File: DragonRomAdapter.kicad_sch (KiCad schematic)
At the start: 8 parts, among them J1 Conn_01x01_Male, U1 68A364, U2 74LVC1G00, U3 28C256

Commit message: tidy-up board
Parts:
- added JP2: Jumper_2_Open, Jumper:SolderJumper-2_P1.3mm_Open_TrianglePad1.0x1.5mm, symbol Jumper:Jumper_2_Open
- J1: now left out of the parts list
- R2, U2: Note (none) -> Not required if JP2 bridged
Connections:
- net ~{E17}: now also JP2.1 (A)
- net ~{E}: now also JP2.2 (B)
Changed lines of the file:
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@@
   )
   (no_connect (at 175.5648 76.3016))
+  (wire (pts (xy 144.8816 24.384) (xy 142.2908 24.384))
+    (stroke (width 0) (type default) (color 0 0 0 0))
+  )
+  (wire (pts (xy 132.1308 24.384) (xy 130.9116 24.384))
+    (stroke (width 0) (type default) (color 0 0 0 0))
+  )
   (wire (pts (xy 136.906 72.644) (xy 137.3124 72.644))
     (stroke (width 0) (type default) (color 0 0 0 0))
@@
   )
   (wire (pts (xy 137.3124 75.438) (xy 137.3124 72.644))
+    (stroke (width 0) (type default) (color 0 0 0 0))
+  )
+  (wire (pts (xy 130.9116 24.384) (xy 130.9116 37.0332))
+    (stroke (width 0) (type default) (color 0 0 0 0))
+  )
+  (wire (pts (xy 144.8816 38.3032) (xy 144.8816 24.384))
     (stroke (width 0) (type default) (color 0 0 0 0))
   )
@@
       (effects (font (size 1.27 1.27)) hide)
     )
+    (property "Note" "Not required if JP2 bridged" (id 4) (at 138.5316 38.3032 0)
+      (effects (font (size 1.27 1.27)) hide)
+    )
     (pin "1")
     (pin "2")
@@
     (pin "1")
   )
+  (symbol (lib_id "Jumper:Jumper_2_Open") (at 137.2108 24.384 0) (unit 1)
+    (in_bom no) (on_board yes) (fields_autoplaced)
+    (property "Reference" "JP2" (id 0) (at 137.2108 17.78 0))
+    (property "Value" "Jumper_2_Open" (id 1) (at 137.2108 20.32 0))
+    (property "Footprint" "Jumper:SolderJumper-2_P1.3mm_Open_TrianglePad1.0x1.5mm" (id 2) (at 137.2108 24.384 0)
+      (effects (font (size 1.27 1.27)) hide)
+    )
+    (property "Datasheet" "~" (id 3) (at 137.2108 24.384 0)
+      (effects (font (size 1.27 1.27)) hide)
+    )
+    (pin "1")
+    (pin "2")
+  )
   (symbol (lib_id "Device:R_Small") (at 134.7724 75.438 270) (unit 1)
     (in_bom yes) (on_board yes)
@@
       (effects (font (size 1.27 1.27)) hide)
     )
+    (property "Note" "Not required if JP2 bridged" (id 4) (at 134.7724 75.438 90)
+      (effects (font (size 1.27 1.27)) hide)
+    )
     (pin "1")
     (pin "2")
@@
   )
   (symbol (lib_id "Connector:Conn_01x01_Male") (at 131.826 72.644 0) (unit 1)
-    (in_bom yes) (on_board yes) (fields_autoplaced)
+    (in_bom no) (on_board yes) (fields_autoplaced)
     (property "Reference" "J1" (id 0) (at 132.461 66.7512 0))
     (property "Value" "Conn_01x01_Male" (id 1) (at 132.461 69.2912 0))
@@
       (reference "JP1") (unit 1) (value "Jumper_3_Bridged12") (footprint "Connector_PinHeader_2.54mm:PinHeader_1x03_P2.54mm_Horizontal")
     )
+    (path "/3828845b-85a6-4ec7-badf-afc34b0893bb"
+      (reference "JP2") (unit 1) (value "Jumper_2_Open") (footprint "Jumper:SolderJumper-2_P1.3mm_Open_TrianglePad1.0x1.5mm")
+    )
     (path "/8595fc95-a608-4da1-ae14-3fc92ad0137b"

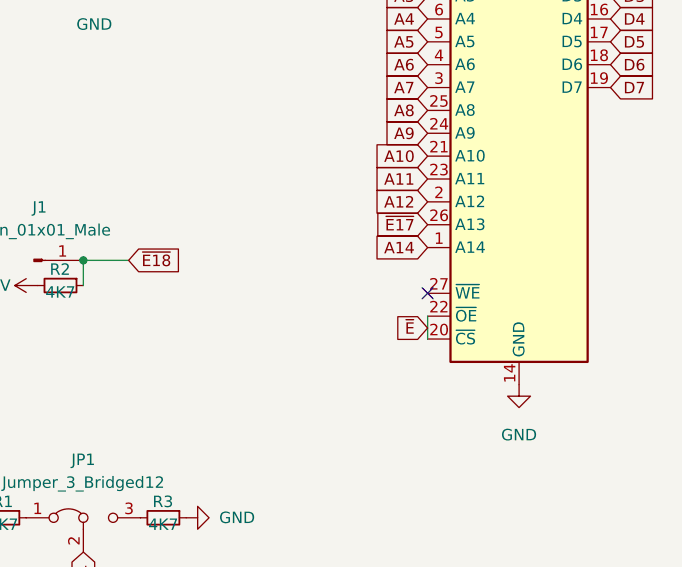
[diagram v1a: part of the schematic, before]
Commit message: use acht logic instead of LVC
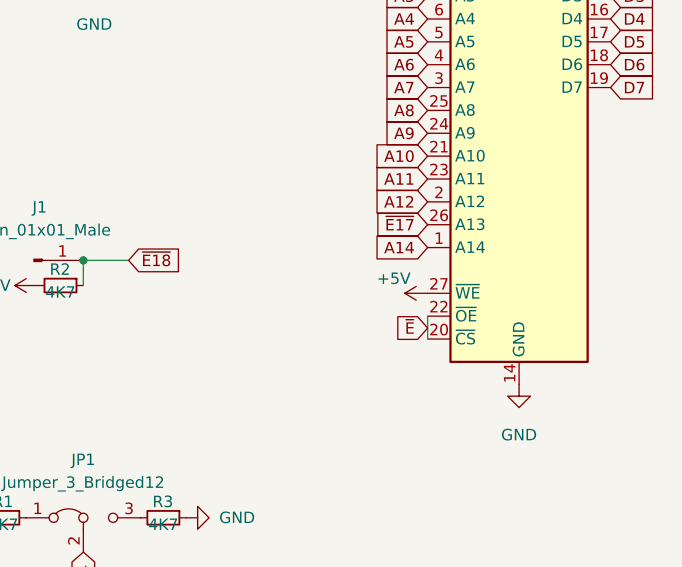
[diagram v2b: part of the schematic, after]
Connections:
- net +5V: now also U3.27 (~{WE})
- no-connect marks 1 -> 0
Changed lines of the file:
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@@
   (junction (at 137.3124 72.644) (diameter 0) (color 0 0 0 0)
   )
-  (no_connect (at 175.5648 76.3016))
   (wire (pts (xy 144.8816 24.384) (xy 142.2908 24.384))
     (stroke (width 0) (type default) (color 0 0 0 0))
@@
     (pin "3")
   )
+  (symbol (lib_id "power:+5V") (at 175.5648 76.3016 90) (unit 1)
+    (in_bom yes) (on_board yes)
+    (property "Reference" "#PWR?" (id 0) (at 179.3748 76.3016 0)
+      (effects (font (size 1.27 1.27)) hide)
+    )
+    (property "Value" "+5V" (id 1) (at 169.926 74.676 90)
+      (effects (font (size 1.27 1.27)) (justify right))
+    )
+    (property "Footprint" "" (id 2) (at 175.5648 76.3016 0)
+      (effects (font (size 1.27 1.27)) hide)
+    )
+    (property "Datasheet" "" (id 3) (at 175.5648 76.3016 0)
+      (effects (font (size 1.27 1.27)) hide)
+    )
+    (pin "1")
+  )
   (symbol (lib_id "Device:R_Small") (at 128.4224 101.2444 270) (unit 1)
     (in_bom yes) (on_board yes)
@@
       (reference "#PWR0106") (unit 1) (value "+5V") (footprint "")
     )
+    (path "/5e38ea97-3af7-4f1d-97a5-960f32b8d19a"
+      (reference "#PWR?") (unit 1) (value "+5V") (footprint "")
+    )
     (path "/9839a238-6b00-4e40-8428-3535b25b1d51"

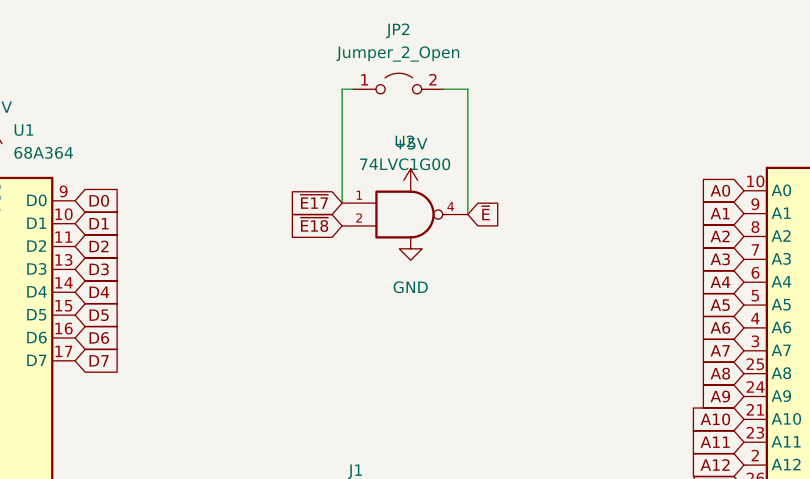
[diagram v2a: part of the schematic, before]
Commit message: migrate to kicad 7
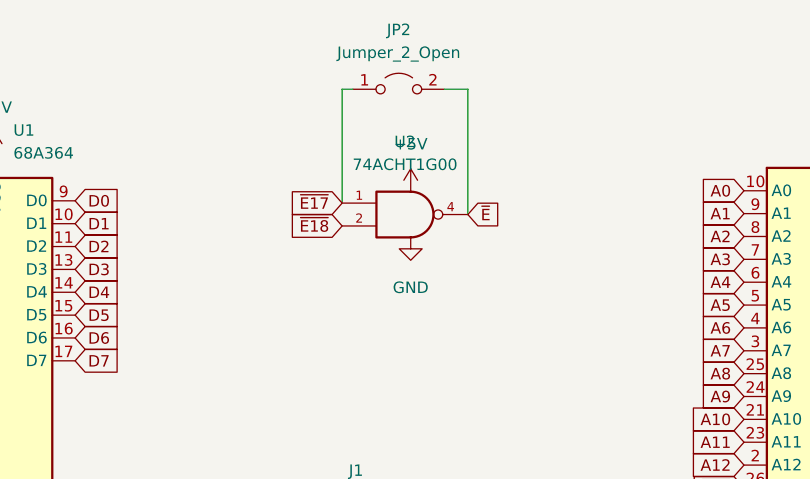
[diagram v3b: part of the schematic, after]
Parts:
- U2: value 74LVC1G00 -> 74ACHT1G00

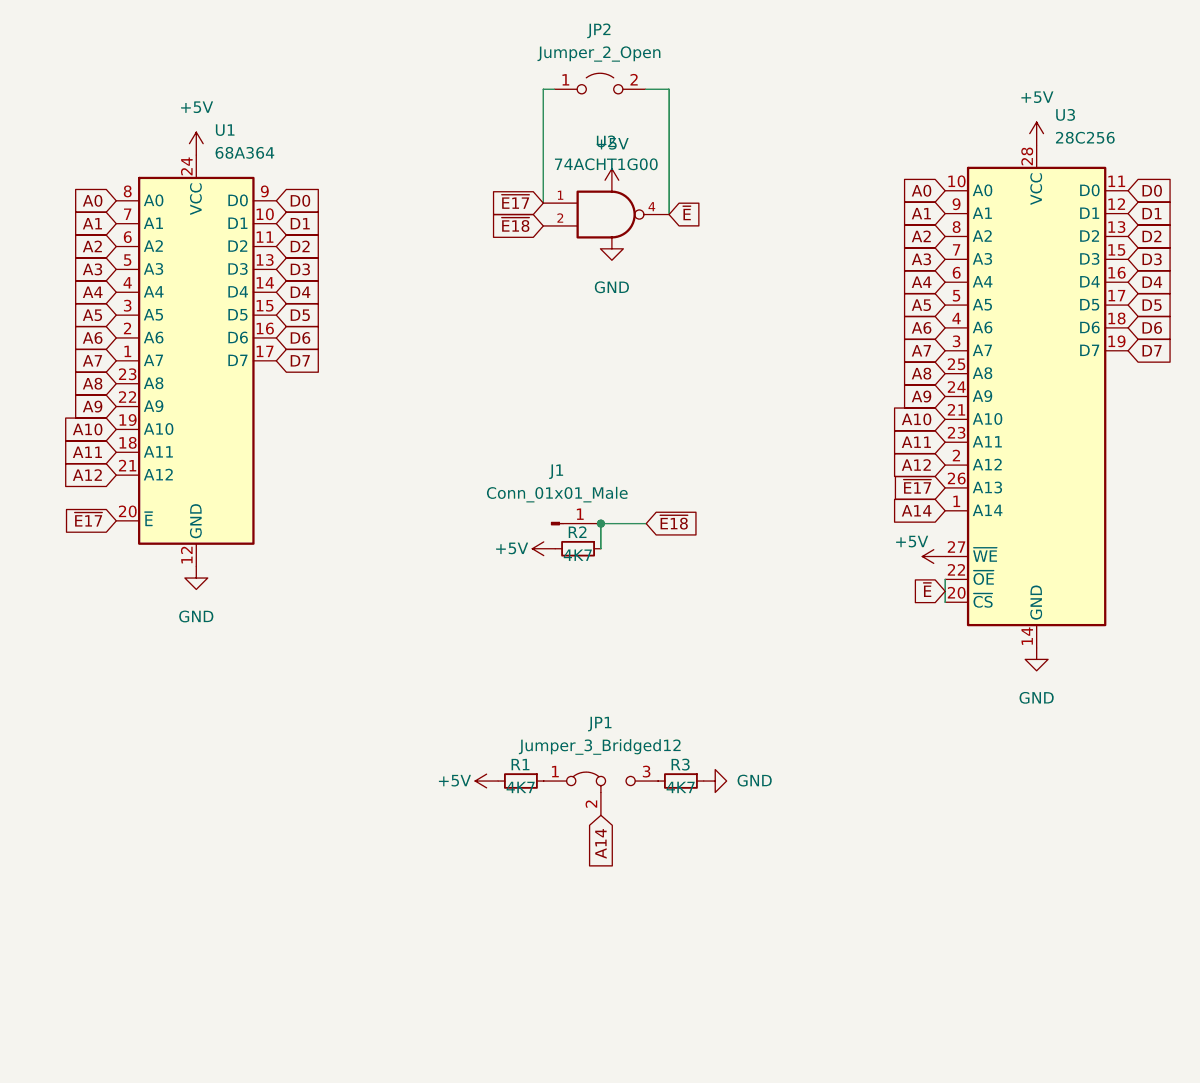
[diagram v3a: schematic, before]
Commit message: make adapter compatible with 28c and 27c roms
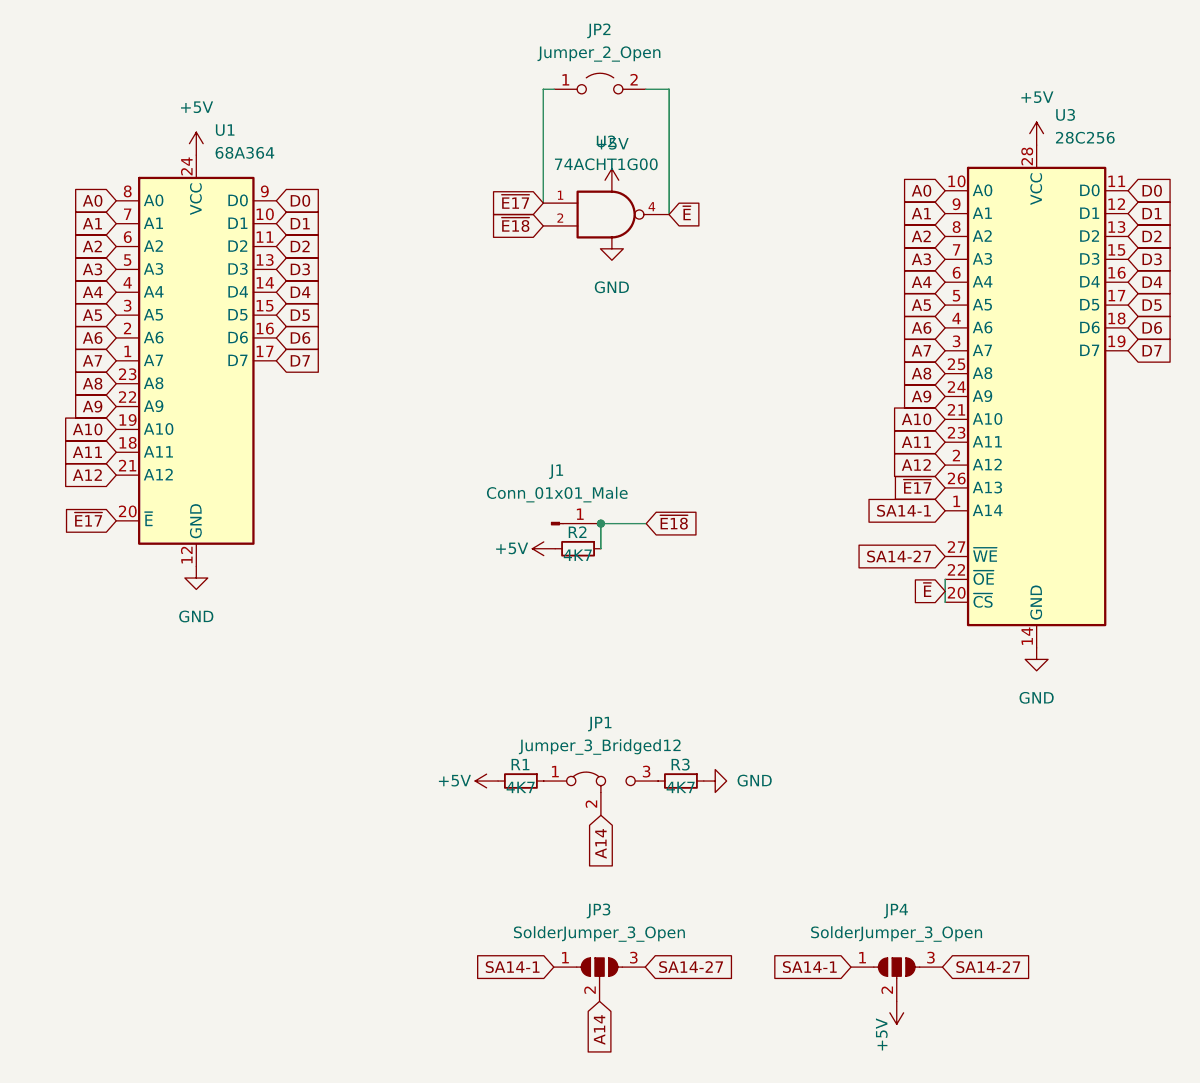
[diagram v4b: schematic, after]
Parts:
- added JP3, JP4: SolderJumper_3_Open, Jumper:SolderJumper-3_P1.3mm_Open_RoundedPad1.0x1.5mm_NumberLabels, symbol Jumper:SolderJumper_3_Open
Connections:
- net +5V: now also JP4.2 (C); no longer U3.27 (~{WE})
- net A14: now also JP3.2 (C); no longer U3.1 (A14)
- new net SA14-1: JP3.1 (A), JP4.1 (A), U3.1 (A14)
- new net SA14-27: JP3.3 (B), JP4.3 (B), U3.27 (~{WE})
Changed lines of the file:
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@@
+    )
+  )
+  (global_label "SA14-27" (shape input) (at 175.5648 76.3016 180) (fields_autoplaced)
+    (effects (font (size 1.27 1.27)) (justify right))
+    (property "Intersheetrefs" "${INTERSHEET_REFS}" (at 163.8711 76.3016 0)
+      (effects (font (size 1.27 1.27)) (justify right) hide)
     )
   )
@@
     )
   )
+  (global_label "SA14-27" (shape input) (at 142.24 121.92 0) (fields_autoplaced)
+    (effects (font (size 1.27 1.27)) (justify left))
+    (property "Intersheetrefs" "${INTERSHEET_REFS}" (at 153.9337 121.92 0)
+      (effects (font (size 1.27 1.27)) (justify left) hide)
+    )
+  )
   (global_label "A3" (shape input) (at 83.4644 44.3992 180) (fields_autoplaced)
     (effects (font (size 1.27 1.27)) (justify right))
@@
     )
   )
+  (global_label "SA14-1" (shape input) (at 132.08 121.92 180) (fields_autoplaced)
+    (effects (font (size 1.27 1.27)) (justify right))
+    (property "Intersheetrefs" "${INTERSHEET_REFS}" (at 121.5958 121.92 0)
+      (effects (font (size 1.27 1.27)) (justify right) hide)
+    )
+  )
   (global_label "A5" (shape input) (at 175.5648 48.3616 180) (fields_autoplaced)
     (effects (font (size 1.27 1.27)) (justify right))
@@
     )
   )
+  (global_label "SA14-27" (shape input) (at 175.26 121.92 0) (fields_autoplaced)
+    (effects (font (size 1.27 1.27)) (justify left))
+    (property "Intersheetrefs" "${INTERSHEET_REFS}" (at 186.9537 121.92 0)
+      (effects (font (size 1.27 1.27)) (justify left) hide)
+    )
+  )
+  (global_label "SA14-1" (shape input) (at 165.1 121.92 180) (fields_autoplaced)
+    (effects (font (size 1.27 1.27)) (justify right))
+    (property "Intersheetrefs" "${INTERSHEET_REFS}" (at 154.6158 121.92 0)
+      (effects (font (size 1.27 1.27)) (justify right) hide)
+    )
+  )
   (global_label "A4" (shape input) (at 83.4644 46.9392 180) (fields_autoplaced)
     (effects (font (size 1.27 1.27)) (justify right))
@@
     )
   )
+  (global_label "A14" (shape input) (at 137.16 125.73 270) (fields_autoplaced)
+    (effects (font (size 1.27 1.27)) (justify right))
+    (property "Intersheetrefs" "${INTERSHEET_REFS}" (at 137.0806 131.6507 90)
+      (effects (font (size 1.27 1.27)) (justify right) hide)
+    )
+  )
   (global_label "A3" (shape input) (at 175.5648 43.2816 180) (fields_autoplaced)
     (effects (font (size 1.27 1.27)) (justify right))
@@
     )
   )
+  (global_label "SA14-1" (shape input) (at 175.5648 71.2216 180) (fields_autoplaced)
+    (effects (font (size 1.27 1.27)) (justify right))
+    (property "Intersheetrefs" "${INTERSHEET_REFS}" (at 165.0806 71.2216 0)
+      (effects (font (size 1.27 1.27)) (justify right) hide)
+    )
+  )
   (global_label "D2" (shape input) (at 101.2444 41.8592 0) (fields_autoplaced)
     (effects (font (size 1.27 1.27)) (justify left))
     (property "Intersheetrefs" "${INTERSHEET_REFS}" (at 106.137 41.7798 0)
       (effects (font (size 1.27 1.27)) (justify left) hide)
-    )
-  )
-  (global_label "A14" (shape input) (at 175.5648 71.2216 180) (fields_autoplaced)
-    (effects (font (size 1.27 1.27)) (justify right))
-    (property "Intersheetrefs" "${INTERSHEET_REFS}" (at 169.6441 71.1422 0)
-      (effects (font (size 1.27 1.27)) (justify right) hide)
     )
   )
@@
     )
   )
-  (symbol (lib_id "power:+5V") (at 175.5648 76.3016 90) (unit 1)
-    (in_bom yes) (on_board yes) (dnp no)
-    (property "Reference" "#PWR0107" (at 179.3748 76.3016 0)
-      (effects (font (size 1.27 1.27)) hide)
-    )
-    (property "Value" "+5V" (at 169.926 74.676 90)
-      (effects (font (size 1.27 1.27)) (justify right))
-    )
-    (property "Footprint" "" (at 175.5648 76.3016 0)
-      (effects (font (size 1.27 1.27)) hide)
-    )
-    (property "Datasheet" "" (at 175.5648 76.3016 0)
-      (effects (font (size 1.27 1.27)) hide)
-    )
-    (pin "1")
-    (instances
-      (project "DragonRomAdapter"
-        (path "/d01bdc37-3f07-4546-8b99-fa04a2624741"
-          (reference "#PWR0107") (unit 1)
-        )
-      )
-    )
-  )
   (symbol (lib_id "Device:R_Small") (at 128.4224 101.2444 270) (unit 1)
     (in_bom yes) (on_board yes) (dnp no)
@@
     )
   )
+  (symbol (lib_id "Jumper:SolderJumper_3_Open") (at 170.18 121.92 0) (unit 1)
+    (in_bom yes) (on_board yes) (dnp no) (fields_autoplaced)
+    (property "Reference" "JP4" (at 170.18 115.57 0)
+      (effects (font (size 1.27 1.27)))
+    )
+    (property "Value" "SolderJumper_3_Open" (at 170.18 118.11 0)
+      (effects (font (size 1.27 1.27)))
+    )
+    (property "Footprint" "Jumper:SolderJumper-3_P1.3mm_Open_RoundedPad1.0x1.5mm_NumberLabels" (at 170.18 121.92 0)
+      (effects (font (size 1.27 1.27)) hide)
+    )
+    (property "Datasheet" "~" (at 170.18 121.92 0)
+      (effects (font (size 1.27 1.27)) hide)
+    )
+    (pin "1")
+    (pin "2")
+    (pin "3")
+    (instances
+      (project "DragonRomAdapter"
+        (path "/d01bdc37-3f07-4546-8b99-fa04a2624741"
+          (reference "JP4") (unit 1)
+        )
+      )
+    )
+  )
   (symbol (lib_id "Connector:Conn_01x01_Male") (at 131.826 72.644 0) (unit 1)
     (in_bom no) (on_board yes) (dnp no) (fields_autoplaced)
@@
     )
   )
+  (symbol (lib_id "power:+5V") (at 170.18 125.73 180) (unit 1)
+    (in_bom yes) (on_board yes) (dnp no)
+    (property "Reference" "#PWR04" (at 170.18 121.92 0)
+      (effects (font (size 1.27 1.27)) hide)
+    )
+    (property "Value" "+5V" (at 168.5544 131.3688 90)
+      (effects (font (size 1.27 1.27)) (justify right))
+    )
+    (property "Footprint" "" (at 170.18 125.73 0)
+      (effects (font (size 1.27 1.27)) hide)
+    )
+    (property "Datasheet" "" (at 170.18 125.73 0)
+      (effects (font (size 1.27 1.27)) hide)
+    )
+    (pin "1")
+    (instances
+      (project "DragonRomAdapter"
+        (path "/d01bdc37-3f07-4546-8b99-fa04a2624741"
+          (reference "#PWR04") (unit 1)
+        )
+      )
+    )
+  )
   (symbol (lib_id "power:GND") (at 148.7424 101.2444 90) (unit 1)
     (in_bom yes) (on_board yes) (dnp no) (fields_autoplaced)
@@
         )
       )
+    )
+  )
+  (symbol (lib_id "Jumper:SolderJumper_3_Open") (at 137.16 121.92 0) (unit 1)
+    (in_bom yes) (on_board yes) (dnp no) (fields_autoplaced)
+    (property "Reference" "JP3" (at 137.16 115.57 0)
+      (effects (font (size 1.27 1.27)))
+    )
+    (property "Value" "SolderJumper_3_Open" (at 137.16 118.11 0)
+      (effects (font (size 1.27 1.27)))
+    )
+    (property "Footprint" "Jumper:SolderJumper-3_P1.3mm_Open_RoundedPad1.0x1.5mm_NumberLabels" (at 137.16 121.92 0)
+      (effects (font (size 1.27 1.27)) hide)
+    )
+    (property "Datasheet" "~" (at 137.16 121.92 0)
+      (effects (font (size 1.27 1.27)) hide)
+    )
+    (pin "1")
+    (pin "2")
+    (pin "3")
+    (instances
+      (project "DragonRomAdapter"
+        (path "/d01bdc37-3f07-4546-8b99-fa04a2624741"
+          (reference "JP3") (unit 1)
+        )
+      )
